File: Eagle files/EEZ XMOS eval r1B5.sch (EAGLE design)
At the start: 224 parts, among them IC1 TPS61169DCKR, IC10 IS42S16400J, IC11 SN74CBTLV3257, IC12 SN74LVC1G02DBVR, IC13 AT25SF041-SSHDT, IC14 SN74CBTLV3257, IC15 TPS2051BDBVR, IC16 TPD2E001DZDR, IC17 TPS561208DDCR, IC18 XE216-512-TQ128-C20, IC19 TPD4E001DRLR, IC2 TPS561208DDCR, IC20 TPD4E001DRLR, IC21 74LVC1G07SE-7, IC22 74LVC1G07SE-7, IC23 TPA6205A1DGN, IC24 DP83848CVV/NOPB, IC26 74VHC595MTC, IC27 PCA21125T/Q900/1,1, IC28 MCP23S17-E/SS, IC29 M95256-WMN6P, IC3 74VHC595MTC, IC4 TPS561208DDCR, IC5 74VHC595MTC, IC6 TPS3808G33DBVR, IC7 AR1021-I/SS, IC8 TPS3808G09DBVR, IC9 74AUP1G74DC.125, J1 678038020, J2 5033981892, Q1 IRLML2246TRPBF, SW1 1301.9316, X1 FC68149, X2 SSW-105-02-S-D, X3 TSW-104-02-S-D_NN, X4 TSW-103-07-F-D, X5 ZL231-20KG, X6 22-23-2021, X7 LMJTAB881243M-L, X8 SSW-107-02-S-D, X9 PCA-6G-20-HL-3 or 52746-2071, Y1 XTAL016178- 85SMX

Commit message: #1, #2
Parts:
- D1: value (none) -> NSR0240
- R13: device rcl:R-EU_R1206 -> rcl:R-EU_R0805
- R14, R24: value 10K -> 1K
- R23: value 56K -> 5K6
- R4: value 34K -> 15K
- R6: value 10K -> 4K7
- R67: value 0R -> N.C.
- R8: value 5K1 -> 2K7
- R9: value 16K -> 10K
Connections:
- net +3V3: now also X2-3.1
- net GND: now also X1.3; no longer X2-3.1
- net N$35: now also IC9A.Q; no longer IC9A.!Q
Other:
- note added: "1 - 2 (Def.)"
- note added: "Ctrl."
- note removed: "1 - 2"
- moved on the sheet: IC9A, R13, X2-1, X2-2, X2-3, X2-4

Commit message: #3
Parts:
- removed ZD1: BZX384-B30.115, EEZ_Lib1:ZENER-DIODESOD323
- added C82: 2u2, rcl:C-EUC0805
- added JP1: 0R-JUMPA, jump-0r-smd:0R-JUMPA
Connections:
- new net N$24: JP1-0R.2, LCD1.RESET
- net !RESET: now also JP1-0R.1; no longer LCD1.RESET
- net +3V3: now also C82.1
- net GND: now also C82.2, JP1-0R.3
- net VLED+: no longer ZD1.C
- net VLED-: no longer ZD1.A
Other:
- note added: "LCD display: RFE43BH-AIW-DNS or RFE430Y-AIW-DNS"
- note removed: "LCD display: RFE43BH-AIW-DNS"
- moved on the sheet: R7

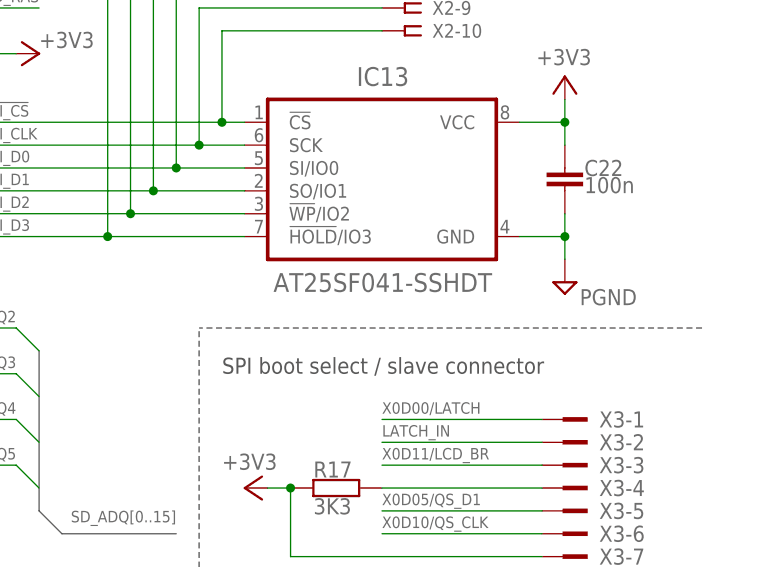
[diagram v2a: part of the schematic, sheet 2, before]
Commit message: fixed flash memory model
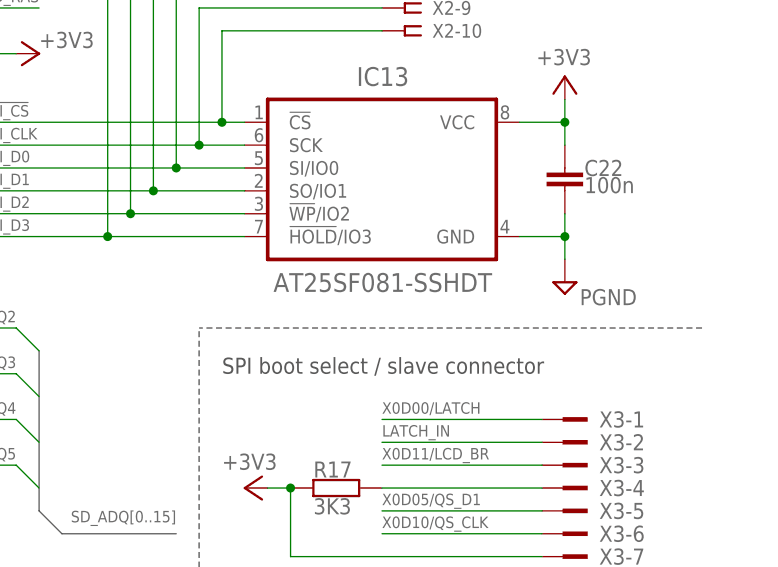
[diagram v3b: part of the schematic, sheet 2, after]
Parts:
- IC13: value AT25SF041-SSHDT -> AT25SF081-SSHDT
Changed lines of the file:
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@@
 <part name="SW1" library="EEZ_Lib1" deviceset="TACT_SW" device="" value="1301.9316"/>
 <part name="FRAME1" library="frames" deviceset="DINA4_L" device=""/>
-<part name="IC13" library="EEZ_Lib1" deviceset="AT25SFXXX" device="" value="AT25SF041-SSHDT"/>
+<part name="IC13" library="EEZ_Lib1" deviceset="AT25SFXXX" device="" value="AT25SF081-SSHDT"/>
 <part name="IC12" library="EEZ_Lib1" deviceset="SN74LVC1G02DBVR" device=""/>
 <part name="IC10" library="EEZ_Lib1" deviceset="IS42S16400" device="" value="IS42S16400J"/>

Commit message: #6
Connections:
- net !SPI0_TOUCH renamed !SPI1_TOUCH
- removed net N$4: C15.1, IC7.Y-, LCD1.YD, R11.2
- new net N$53: C15.1, IC7.Y-, LCD1.YD
- net +3V3: now also IC7.M1
- net GND: now also IC7.M2; no longer IC7.M1
- net N$3: now also R11.2
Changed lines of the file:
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@@
 <setting verticaltext="up"/>
 </settings>
-<grid distance="0.1" unitdist="inch" unit="inch" style="lines" multiple="1" display="no" altdistance="0.01" altunitdist="inch" altunit="inch"/>
+<grid distance="0.025" unitdist="inch" unit="inch" style="lines" multiple="1" display="no" altdistance="0.01" altunitdist="inch" altunit="inch"/>
 <layers>
 <layer number="1" name="Top" color="4" fill="1" visible="no" active="no"/>
@@
 <pinref part="+3V3" gate="G$1" pin="+3V3"/>
 <wire x1="71.12" y1="50.8" x2="71.12" y2="55.88" width="0.1524" layer="91"/>
+<wire x1="71.12" y1="50.8" x2="81.28" y2="50.8" width="0.1524" layer="91"/>
+<wire x1="81.28" y1="50.8" x2="81.28" y2="38.1" width="0.1524" layer="91"/>
+<pinref part="IC7" gate="A" pin="M1"/>
+<wire x1="81.28" y1="38.1" x2="60.96" y2="38.1" width="0.1524" layer="91"/>
 </segment>
 <segment>
@@
 <pinref part="SUPPLY7" gate="GND" pin="GND"/>
 <junction x="71.12" y="43.18"/>
-<pinref part="IC7" gate="A" pin="M1"/>
-<wire x1="60.96" y1="38.1" x2="63.5" y2="38.1" width="0.1524" layer="91"/>
-<wire x1="63.5" y1="38.1" x2="63.5" y2="43.18" width="0.1524" layer="91"/>
+<pinref part="IC7" gate="A" pin="M2"/>
+<wire x1="60.96" y1="35.56" x2="63.5" y2="35.56" width="0.1524" layer="91"/>
+<wire x1="63.5" y1="35.56" x2="63.5" y2="43.18" width="0.1524" layer="91"/>
 <junction x="63.5" y="43.18"/>
 </segment>
@@
 <pinref part="IC7" gate="A" pin="X-"/>
 <wire x1="30.48" y1="38.1" x2="20.32" y2="38.1" width="0.1524" layer="91"/>
-<wire x1="20.32" y1="38.1" x2="7.62" y2="38.1" width="0.1524" layer="91"/>
+<wire x1="20.32" y1="38.1" x2="15.24" y2="38.1" width="0.1524" layer="91"/>
+<wire x1="15.24" y1="38.1" x2="7.62" y2="38.1" width="0.1524" layer="91"/>
 <wire x1="7.62" y1="38.1" x2="7.62" y2="71.12" width="0.1524" layer="91"/>
 <pinref part="LCD1" gate="G$1" pin="XL"/>
@@
 <wire x1="20.32" y1="30.48" x2="20.32" y2="38.1" width="0.1524" layer="91"/>
 <junction x="20.32" y="38.1"/>
-</segment>
-</net>
-<net name="N$4" class="0">
-<segment>
-<pinref part="IC7" gate="A" pin="Y-"/>
-<wire x1="30.48" y1="40.64" x2="15.24" y2="40.64" width="0.1524" layer="91"/>
-<wire x1="15.24" y1="40.64" x2="10.16" y2="40.64" width="0.1524" layer="91"/>
-<wire x1="10.16" y1="40.64" x2="10.16" y2="73.66" width="0.1524" layer="91"/>
-<pinref part="LCD1" gate="G$1" pin="YD"/>
-<wire x1="10.16" y1="73.66" x2="35.56" y2="73.66" width="0.1524" layer="91"/>
-<pinref part="C15" gate="G$1" pin="1"/>
-<wire x1="10.16" y1="30.48" x2="10.16" y2="40.64" width="0.1524" layer="91"/>
-<junction x="10.16" y="40.64"/>
+<wire x1="15.24" y1="38.1" x2="15.24" y2="48.26" width="0.1524" layer="91"/>
+<junction x="15.24" y="38.1"/>
 <pinref part="R11" gate="G$1" pin="2"/>
-<wire x1="17.78" y1="48.26" x2="15.24" y2="48.26" width="0.1524" layer="91"/>
-<wire x1="15.24" y1="48.26" x2="15.24" y2="40.64" width="0.1524" layer="91"/>
-<junction x="15.24" y="40.64"/>
+<wire x1="15.24" y1="48.26" x2="17.78" y2="48.26" width="0.1524" layer="91"/>
 </segment>
 </net>
@@
 </segment>
 </net>
-<net name="!SPI0_TOUCH" class="0">
+<net name="!SPI1_TOUCH" class="0">
 <segment>
 <pinref part="IC7" gate="A" pin="SS"/>
@@
 </segment>
 </net>
+<net name="N$53" class="0">
+<segment>
+<pinref part="IC7" gate="A" pin="Y-"/>
+<wire x1="30.48" y1="40.64" x2="10.16" y2="40.64" width="0.1524" layer="91"/>
+<pinref part="LCD1" gate="G$1" pin="YD"/>
+<wire x1="10.16" y1="40.64" x2="10.16" y2="73.66" width="0.1524" layer="91"/>
+<wire x1="10.16" y1="73.66" x2="35.56" y2="73.66" width="0.1524" layer="91"/>
+<pinref part="C15" gate="G$1" pin="1"/>
+<wire x1="10.16" y1="30.48" x2="10.16" y2="40.64" width="0.1524" layer="91"/>
+<junction x="10.16" y="40.64"/>
+</segment>
+</net>
 </nets>
 </sheet>
@@
 </segment>
 </net>
-<net name="!SPI0_TOUCH" class="0">
+<net name="!SPI1_TOUCH" class="0">
 <segment>
 <pinref part="IC18" gate="-TILE0" pin="X0D37"/>
@@
 <instance part="IC29" gate="G$1" x="93.98" y="154.94" smashed="yes">
 <attribute name="NAME" x="90.5256" y="168.5036" size="2.0828" layer="95" ratio="10" rot="SR0"/>
-<attribute name="VALUE" x="87.9856" y="146.2532" size="2.0828" layer="96" ratio="10" rot="SR0"/>
+<attribute name="VALUE" x="82.9056" y="141.8082" size="2.0828" layer="96" ratio="10" rot="SR0"/>
 </instance>
 </instances>

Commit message: #7
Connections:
- net +3V3: now also R51.1, R52.1
- net GND: no longer R51.1, R52.1
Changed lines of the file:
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@@
 <setting verticaltext="up"/>
 </settings>
-<grid distance="0.025" unitdist="inch" unit="inch" style="lines" multiple="1" display="no" altdistance="0.01" altunitdist="inch" altunit="inch"/>
+<grid distance="0.1" unitdist="inch" unit="inch" style="lines" multiple="1" display="no" altdistance="0.01" altunitdist="inch" altunit="inch"/>
 <layers>
 <layer number="1" name="Top" color="4" fill="1" visible="no" active="no"/>
@@
 <part name="C82" library="rcl" deviceset="C-EU" device="C0805" value="2u2"/>
 <part name="JP1" library="jump-0r-smd" deviceset="0R-JUMP" device="A"/>
+<part name="+3V53" library="supply1" deviceset="+3V3" device=""/>
 </parts>
 <sheets>
@@
 <attribute name="VALUE" x="39.37" y="27.559" size="1.4224" layer="96"/>
 </instance>
+<instance part="+3V53" gate="G$1" x="142.24" y="35.56" smashed="yes" rot="R180">
+<attribute name="VALUE" x="145.415" y="34.925" size="1.778" layer="96" rot="R180"/>
+</instance>
 </instances>
 <busses>
@@
 <wire x1="180.34" y1="43.18" x2="180.34" y2="40.64" width="0.1524" layer="91"/>
 <junction x="180.34" y="40.64"/>
-<pinref part="R52" gate="G$1" pin="1"/>
-<wire x1="149.86" y1="40.64" x2="142.24" y2="40.64" width="0.1524" layer="91"/>
-<wire x1="142.24" y1="40.64" x2="142.24" y2="43.18" width="0.1524" layer="91"/>
-<junction x="149.86" y="40.64"/>
-<pinref part="R51" gate="G$1" pin="1"/>
-<wire x1="142.24" y1="40.64" x2="139.7" y2="40.64" width="0.1524" layer="91"/>
-<wire x1="139.7" y1="40.64" x2="139.7" y2="43.18" width="0.1524" layer="91"/>
-<junction x="142.24" y="40.64"/>
 <wire x1="160.02" y1="43.18" x2="160.02" y2="40.64" width="0.1524" layer="91"/>
 <junction x="160.02" y="40.64"/>
@@
 <wire x1="101.6" y1="127" x2="101.6" y2="129.54" width="0.1524" layer="91"/>
 </segment>
+<segment>
+<pinref part="R51" gate="G$1" pin="1"/>
+<pinref part="R52" gate="G$1" pin="1"/>
+<wire x1="142.24" y1="40.64" x2="142.24" y2="43.18" width="0.1524" layer="91"/>
+<wire x1="142.24" y1="40.64" x2="139.7" y2="40.64" width="0.1524" layer="91"/>
+<wire x1="139.7" y1="40.64" x2="139.7" y2="43.18" width="0.1524" layer="91"/>
+<pinref part="+3V53" gate="G$1" pin="+3V3"/>
+<wire x1="142.24" y1="38.1" x2="142.24" y2="40.64" width="0.1524" layer="91"/>
+<junction x="142.24" y="40.64"/>
+</segment>
 </net>

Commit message: #8
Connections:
- net !SPI1_SDCARD: now also J2.CD/DAT3; no longer J2.DAT2
- net +3V3: now also J2.VDD; no longer J2.CMD
- net GND: now also J2.VSS; no longer J2.CLK
- net SPI1_CLK: now also J2.CLK; no longer J2.VDD
- net SPI1_MISO: now also J2.DAT0; no longer J2.VSS
- net SPI1_MOSI: now also J2.CMD; no longer J2.CD/DAT3
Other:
- moved on the sheet: J2
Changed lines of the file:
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@@
 <part name="R17" library="rcl" deviceset="R-EU_" device="R0805" value="3K3"/>
 <part name="+3V50" library="supply1" deviceset="+3V3" device=""/>
-<part name="J2" library="EEZ_Lib1" deviceset="5033981892" device=""/>
 <part name="SUPPLY92" library="supply2" deviceset="GND" device=""/>
 <part name="+3V51" library="supply1" deviceset="+3V3" device=""/>
@@
 <part name="JP1" library="jump-0r-smd" deviceset="0R-JUMP" device="A"/>
 <part name="+3V53" library="supply1" deviceset="+3V3" device=""/>
+<part name="J2" library="EEZ_Lib1" deviceset="5033981892" device=""/>
 </parts>
 <sheets>
@@
 <attribute name="VALUE" x="131.445" y="142.875" size="1.778" layer="96" rot="R180"/>
 </instance>
-<instance part="SUPPLY116" gate="GND" x="177.8" y="157.48" smashed="yes">
-<attribute name="VALUE" x="179.705" y="155.575" size="1.778" layer="96" rot="R180"/>
+<instance part="SUPPLY116" gate="GND" x="177.8" y="160.02" smashed="yes">
+<attribute name="VALUE" x="179.705" y="158.115" size="1.778" layer="96" rot="R180"/>
 </instance>
 <instance part="C76" gate="G$1" x="114.3" y="162.56" smashed="yes" rot="R90">
@@
 <attribute name="VALUE" x="241.3" y="125.73" size="1.27" layer="96" rot="R90"/>
 </instance>
-<instance part="J2" gate="G$1" x="162.56" y="152.4"/>
 <instance part="SUPPLY92" gate="GND" x="177.8" y="134.62" smashed="yes">
 <attribute name="VALUE" x="179.705" y="132.715" size="1.778" layer="96" rot="R180"/>
@@
 <attribute name="VALUE" x="82.9056" y="141.8082" size="2.0828" layer="96" ratio="10" rot="SR0"/>
 </instance>
+<instance part="J2" gate="G$1" x="162.56" y="154.94" smashed="yes">
+<attribute name="NAME" x="152.4" y="170.815" size="1.778" layer="95"/>
+<attribute name="VALUE" x="152.4" y="137.16" size="1.778" layer="96"/>
+</instance>
 </instances>
 <busses>
@@
 <wire x1="129.54" y1="157.48" x2="127" y2="157.48" width="0.1524" layer="91"/>
 <junction x="129.54" y="157.48"/>
-<pinref part="J2" gate="G$1" pin="CMD"/>
+<pinref part="J2" gate="G$1" pin="VDD"/>
 </segment>
 </net>
@@
 <wire x1="127" y1="149.86" x2="129.54" y2="149.86" width="0.1524" layer="91"/>
 <junction x="129.54" y="149.86"/>
-<pinref part="J2" gate="G$1" pin="CLK"/>
+<pinref part="J2" gate="G$1" pin="VSS"/>
 </segment>
 <segment>
 <pinref part="SUPPLY116" gate="GND" pin="GND"/>
-<wire x1="177.8" y1="160.02" x2="177.8" y2="162.56" width="0.1524" layer="91"/>
+<wire x1="177.8" y1="162.56" x2="177.8" y2="165.1" width="0.1524" layer="91"/>
+<wire x1="175.26" y1="165.1" x2="177.8" y2="165.1" width="0.1524" layer="91"/>
 <pinref part="J2" gate="G$1" pin="SH"/>
-<wire x1="175.26" y1="162.56" x2="177.8" y2="162.56" width="0.1524" layer="91"/>
 </segment>
 <segment>
@@
 </segment>
 <segment>
-<pinref part="J2" gate="G$1" pin="SW2"/>
-<wire x1="175.26" y1="139.7" x2="177.8" y2="139.7" width="0.1524" layer="91"/>
+<wire x1="175.26" y1="142.24" x2="177.8" y2="142.24" width="0.1524" layer="91"/>
 <pinref part="SUPPLY92" gate="GND" pin="GND"/>
-<wire x1="177.8" y1="139.7" x2="177.8" y2="137.16" width="0.1524" layer="91"/>
+<wire x1="177.8" y1="142.24" x2="177.8" y2="137.16" width="0.1524" layer="91"/>
+<pinref part="J2" gate="G$1" pin="SW2"/>
 </segment>
 </net>
@@
 <wire x1="149.86" y1="162.56" x2="137.16" y2="162.56" width="0.1524" layer="91"/>
 <label x="137.16" y="163.195" size="1.27" layer="102"/>
-<pinref part="J2" gate="G$1" pin="DAT2"/>
+<pinref part="J2" gate="G$1" pin="CD/DAT3"/>
 </segment>
 </net>
@@
 <wire x1="149.86" y1="154.94" x2="137.16" y2="154.94" width="0.1524" layer="91"/>
 <label x="137.16" y="155.575" size="1.27" layer="102"/>
-<pinref part="J2" gate="G$1" pin="VDD"/>
+<pinref part="J2" gate="G$1" pin="CLK"/>
 </segment>
 <segment>
@@
 <wire x1="149.86" y1="149.86" x2="137.16" y2="149.86" width="0.1524" layer="91"/>
 <label x="137.16" y="150.495" size="1.27" layer="102"/>
-<pinref part="J2" gate="G$1" pin="VSS"/>
+<pinref part="J2" gate="G$1" pin="DAT0"/>
 </segment>
 <segment>
@@
 <wire x1="149.86" y1="160.02" x2="137.16" y2="160.02" width="0.1524" layer="91"/>
 <label x="137.16" y="160.655" size="1.27" layer="102"/>
-<pinref part="J2" gate="G$1" pin="CD/DAT3"/>
+<pinref part="J2" gate="G$1" pin="CMD"/>
 </segment>
 <segment>
@@
 </segment>
 <segment>
-<wire x1="149.86" y1="139.7" x2="137.16" y2="139.7" width="0.1524" layer="91"/>
-<label x="137.16" y="140.335" size="1.27" layer="102"/>
+<wire x1="149.86" y1="142.24" x2="137.16" y2="142.24" width="0.1524" layer="91"/>
+<label x="137.16" y="142.875" size="1.27" layer="102"/>
 <pinref part="J2" gate="G$1" pin="SW1"/>
 </segment>
